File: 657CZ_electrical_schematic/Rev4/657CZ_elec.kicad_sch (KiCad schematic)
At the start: 44 parts, among them M2 Starter, SW1 E-Bus Alt Feed, SW13 E IGN, SW14 M IGN, SW2 Aux Alt Off/On, SW5 BATT/ALT DC POWER

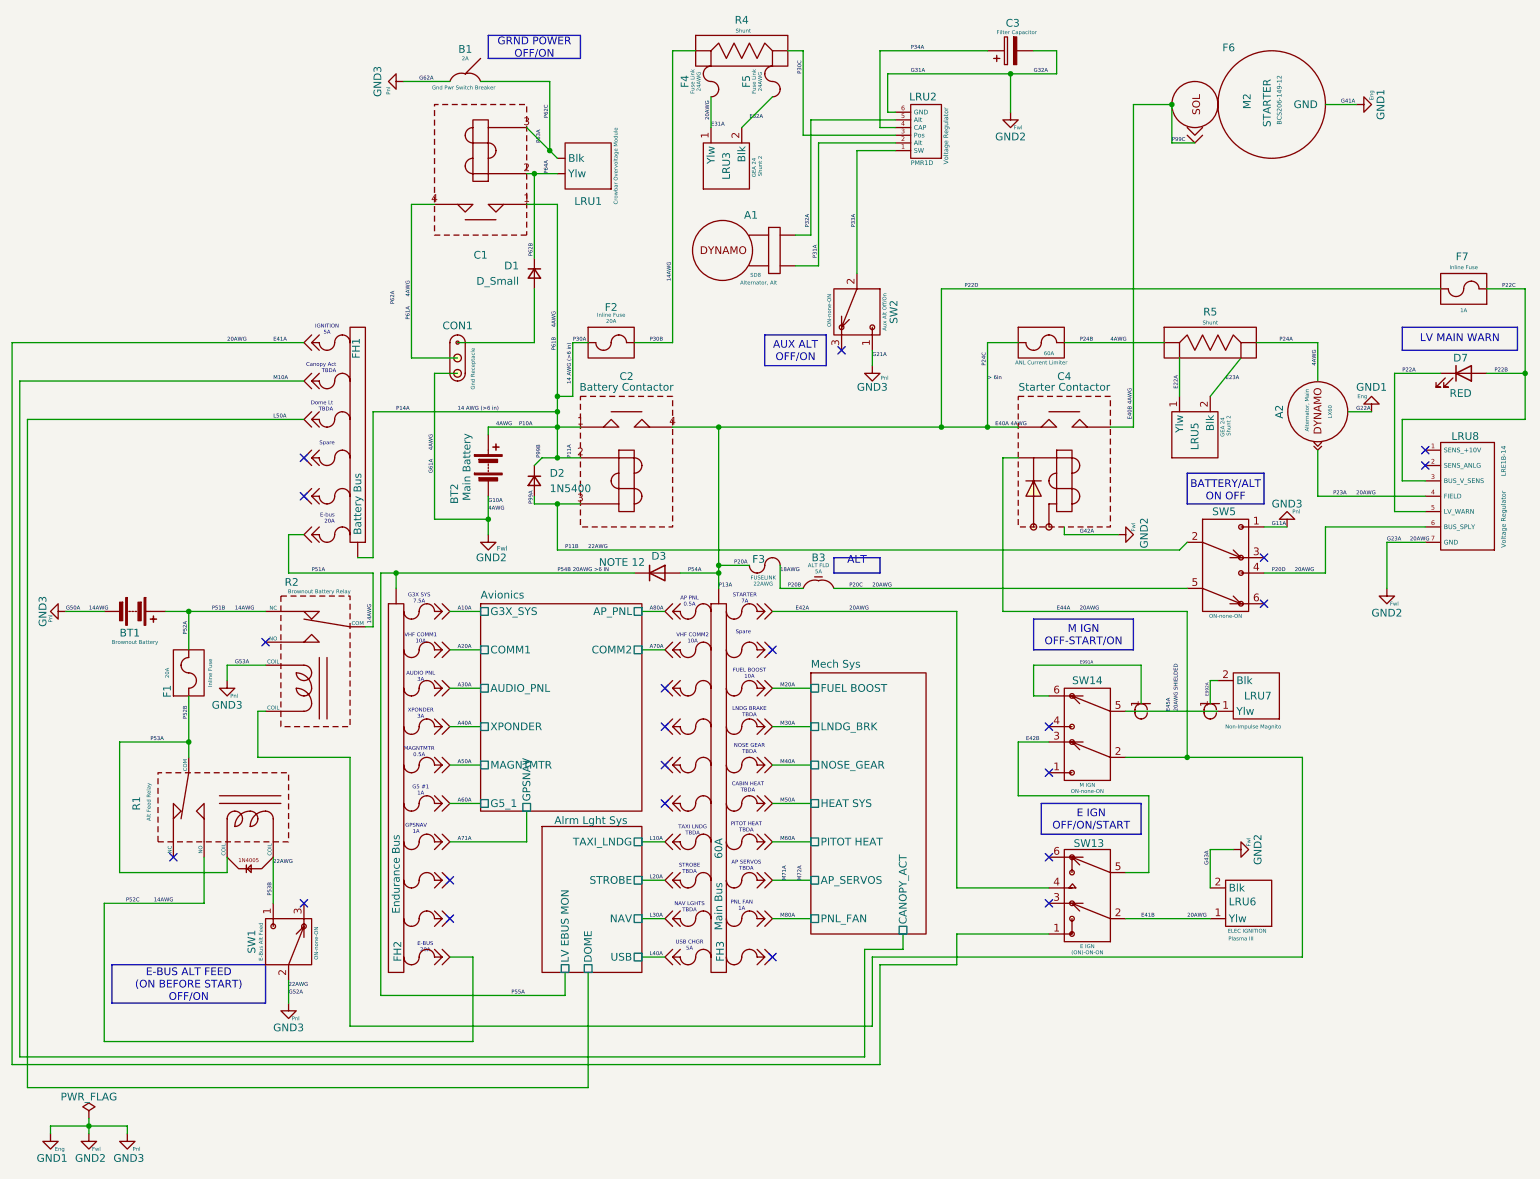
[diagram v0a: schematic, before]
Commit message: corrected comm1,2 to main/ebus, connected lightspeed to ebus
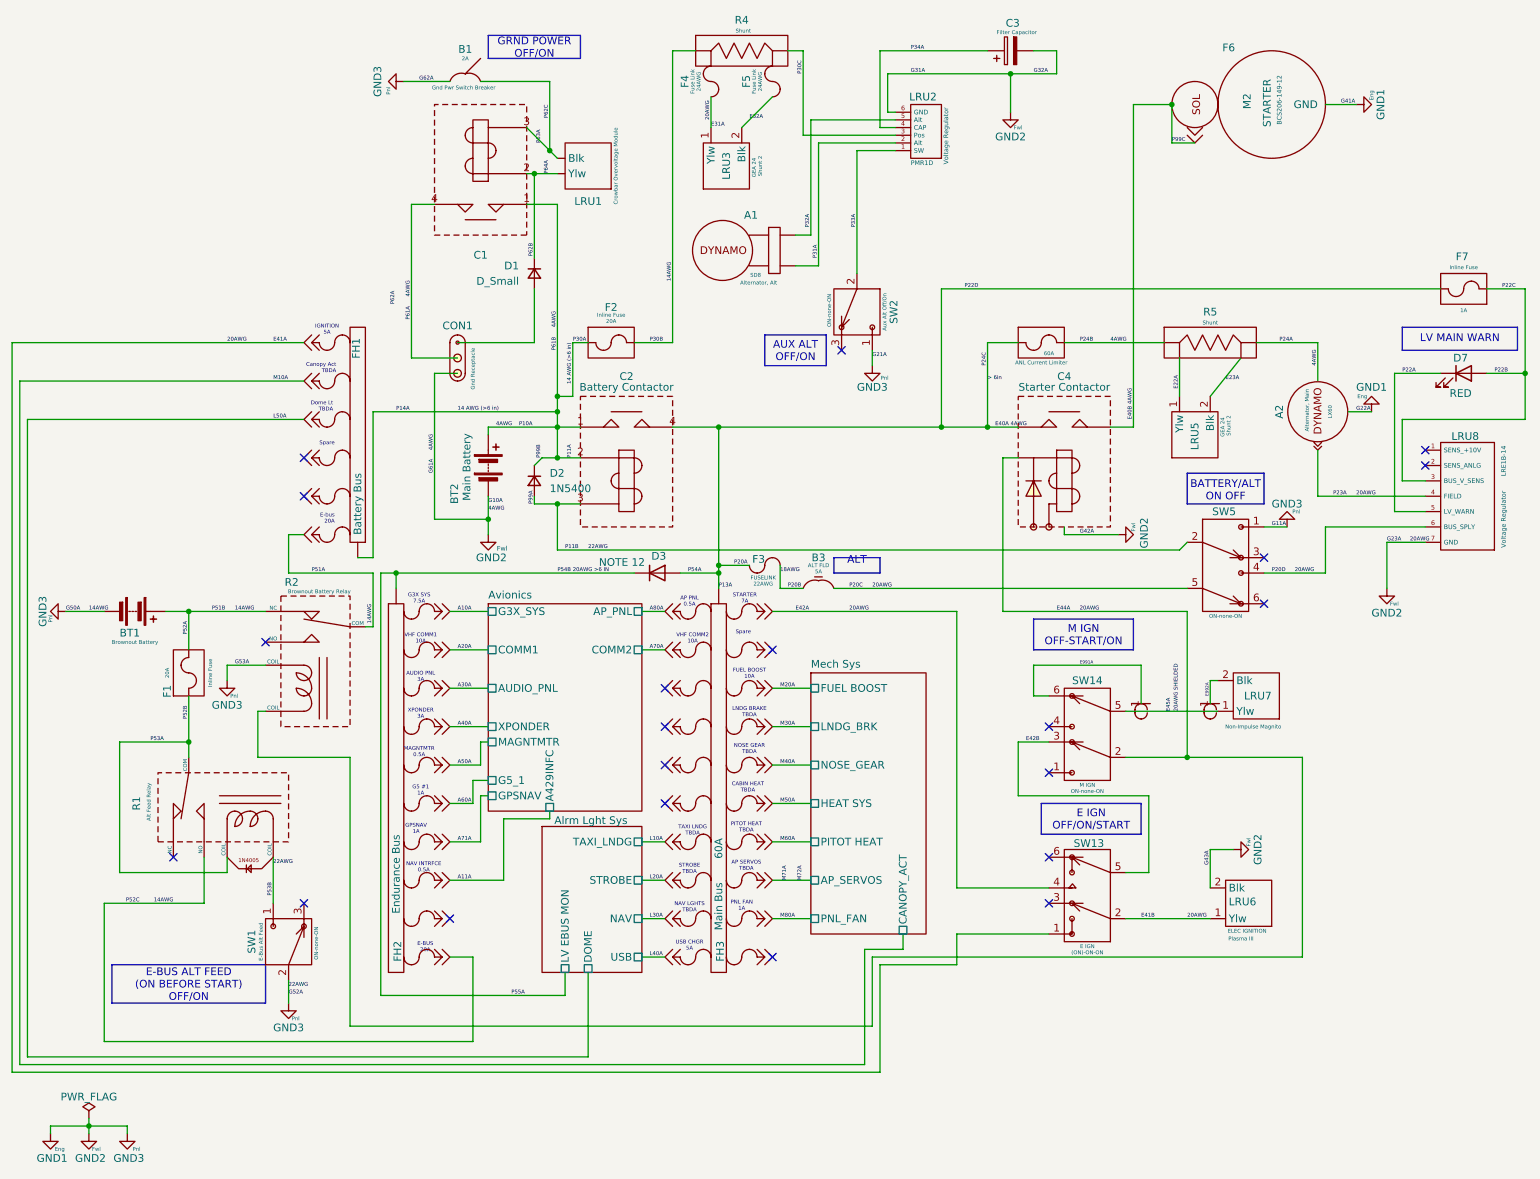
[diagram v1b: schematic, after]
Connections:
- net A11A: now reaches FH2.9 (Desc)
- no-connect marks 22 -> 21
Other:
- sheet Avionics ports: added A429INFC; removed none
- note added: "NAV INTRFCE 0.5A"
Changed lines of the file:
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@@
 		)
 	)
+	(text "NAV INTRFCE\n0.5A"
+		(exclude_from_sim no)
+		(at 82.042 154.178 0)
+		(effects
+			(font
+				(size 0.635 0.635)
+			)
+		)
+	)
 	(text "AP PNL\n0.5A"
 		(exclude_from_sim no)
@@
 	)
 	(no_connect
-		(at 86.36 156.21)
-	)
-	(no_connect
 		(at 62.23 92.71)
 	)
@@
 	(wire
 		(pts
-			(xy 13.97 186.69) (xy 157.48 186.69)
+			(xy 13.97 187.96) (xy 157.48 187.96)
 		)
 		(stroke
@@
 	(wire
 		(pts
-			(xy 86.36 143.51) (xy 91.44 143.51)
+			(xy 86.36 156.21) (xy 95.25 156.21)
+		)
+		(stroke
+			(width 0)
+			(type default)
+		)
+	)
+	(wire
+		(pts
+			(xy 90.17 139.7) (xy 92.71 139.7)
 		)
 		(stroke
@@
 	(wire
 		(pts
-			(xy 86.36 149.86) (xy 99.06 149.86)
+			(xy 86.36 149.86) (xy 91.44 149.86)
 		)
 		(stroke
@@
 	(wire
 		(pts
+			(xy 91.44 133.35) (xy 91.44 137.16)
+		)
+		(stroke
+			(width 0)
+			(type default)
+		)
+	)
+	(wire
+		(pts
 			(xy 100.33 39.37) (xy 104.14 39.37)
 		)
@@
 	(wire
 		(pts
-			(xy 86.36 118.11) (xy 91.44 118.11)
+			(xy 86.36 118.11) (xy 92.71 118.11)
 		)
 		(stroke
@@
 	(wire
 		(pts
-			(xy 154.94 167.64) (xy 154.94 185.42)
+			(xy 154.94 167.64) (xy 154.94 186.69)
 		)
 		(stroke
@@
 	(wire
 		(pts
-			(xy 16.51 190.5) (xy 109.22 190.5)
+			(xy 16.51 185.42) (xy 109.22 185.42)
+		)
+		(stroke
+			(width 0)
+			(type default)
+		)
+	)
+	(wire
+		(pts
+			(xy 95.25 146.05) (xy 102.87 146.05)
 		)
 		(stroke
@@
 	(wire
 		(pts
-			(xy 86.36 111.76) (xy 91.44 111.76)
+			(xy 86.36 111.76) (xy 92.71 111.76)
 		)
 		(stroke
@@
 	(wire
 		(pts
-			(xy 86.36 137.16) (xy 91.44 137.16)
+			(xy 91.44 133.35) (xy 92.71 133.35)
 		)
 		(stroke
@@
 	(wire
 		(pts
-			(xy 15.24 73.66) (xy 15.24 185.42)
+			(xy 15.24 73.66) (xy 15.24 186.69)
 		)
 		(stroke
@@
 	(wire
 		(pts
-			(xy 154.94 185.42) (xy 15.24 185.42)
+			(xy 154.94 186.69) (xy 15.24 186.69)
 		)
 		(stroke
@@
 	(wire
 		(pts
-			(xy 16.51 80.01) (xy 16.51 190.5)
+			(xy 16.51 80.01) (xy 16.51 185.42)
 		)
 		(stroke
@@
 	(wire
 		(pts
+			(xy 91.44 137.16) (xy 86.36 137.16)
+		)
+		(stroke
+			(width 0)
+			(type default)
+		)
+	)
+	(wire
+		(pts
 			(xy 54.61 128.27) (xy 54.61 135.89)
 		)
@@
 	(wire
 		(pts
+			(xy 90.17 139.7) (xy 90.17 143.51)
+		)
+		(stroke
+			(width 0)
+			(type default)
+		)
+	)
+	(wire
+		(pts
 			(xy 227.33 168.91) (xy 156.21 168.91)
 		)
@@
 	(wire
 		(pts
-			(xy 86.36 124.46) (xy 91.44 124.46)
+			(xy 86.36 124.46) (xy 92.71 124.46)
 		)
 		(stroke
@@
 	(wire
 		(pts
+			(xy 91.44 142.24) (xy 92.71 142.24)
+		)
+		(stroke
+			(width 0)
+			(type default)
+		)
+	)
+	(wire
+		(pts
+			(xy 102.87 146.05) (xy 102.87 144.78)
+		)
+		(stroke
+			(width 0)
+			(type default)
+		)
+	)
+	(wire
+		(pts
 			(xy 13.97 67.31) (xy 62.23 67.31)
 		)
@@
 	(wire
 		(pts
-			(xy 13.97 186.69) (xy 13.97 67.31)
+			(xy 13.97 187.96) (xy 13.97 67.31)
 		)
 		(stroke
@@
 	(wire
 		(pts
-			(xy 99.06 149.86) (xy 99.06 144.78)
+			(xy 91.44 149.86) (xy 91.44 142.24)
 		)
 		(stroke
@@
 	(wire
 		(pts
+			(xy 90.17 143.51) (xy 86.36 143.51)
+		)
+		(stroke
+			(width 0)
+			(type default)
+		)
+	)
+	(wire
+		(pts
 			(xy 247.65 95.25) (xy 242.57 95.25)
 		)
@@
 	(wire
 		(pts
-			(xy 86.36 130.81) (xy 91.44 130.81)
+			(xy 86.36 130.81) (xy 92.71 130.81)
 		)
 		(stroke
@@
 	(wire
 		(pts
-			(xy 109.22 190.5) (xy 109.22 171.45)
+			(xy 109.22 185.42) (xy 109.22 171.45)
 		)
 		(stroke
@@
 	(wire
 		(pts
+			(xy 95.25 156.21) (xy 95.25 146.05)
+		)
+		(stroke
+			(width 0)
+			(type default)
+		)
+	)
+	(wire
+		(pts
 			(xy 187.96 67.31) (xy 204.47 67.31)
 		)
@@
 	(wire
 		(pts
-			(xy 157.48 170.18) (xy 157.48 186.69)
+			(xy 157.48 170.18) (xy 157.48 187.96)
 		)
 		(stroke
@@
 		)
 	)
+	(label "A11A"
+		(at 87.63 156.21 0)
+		(effects
+			(font
+				(size 0.635 0.635)
+			)
+			(justify left bottom)
+		)
+	)
 	(label "E42A"
 		(at 143.51 111.76 0)
@@
 	)
 	(sheet
-		(at 91.44 110.49)
-		(size 26.67 34.29)
+		(at 92.71 110.49)
+		(size 25.4 34.29)
 		(exclude_from_sim no)
 		(in_bom yes)
@@
 		)
 		(property "Sheetname" "Avionics"
-			(at 91.44 109.7784 0)
+			(at 92.71 109.7784 0)
 			(effects
 				(font
@@
 		)
 		(property "Sheetfile" "avionics.kicad_sch"
-			(at 91.44 145.3646 0)
+			(at 92.71 145.3646 0)
 			(effects
 				(font
@@
 		)
 		(pin "AUDIO_PNL" passive
-			(at 91.44 124.46 180)
+			(at 92.71 124.46 180)
 			(effects
 				(font
@@
 		)
 		(pin "XPONDER" passive
-			(at 91.44 130.81 180)
+			(at 92.71 130.81 180)
 			(effects
 				(font
@@
 		)
 		(pin "MAGNTMTR" passive
-			(at 91.44 137.16 180)
+			(at 92.71 133.35 180)
 			(effects
 				(font
@@
 		)
 		(pin "G3X_SYS" passive
-			(at 91.44 111.76 180)
+			(at 92.71 111.76 180)
 			(effects
 				(font
@@
 		)
 		(pin "G5_1" passive
-			(at 91.44 143.51 180)
+			(at 92.71 139.7 180)
 			(effects
 				(font
@@
 		)
 		(pin "COMM1" passive
-			(at 91.44 118.11 180)
+			(at 92.71 118.11 180)
 			(effects
 				(font
@@
 		)
 		(pin "GPSNAV" passive
-			(at 99.06 144.78 270)
+			(at 92.71 142.24 180)
+			(effects
+				(font
+					(size 1.27 1.27)
+				)
+				(justify left)
+			)
+		)
+		(pin "A429INFC" passive
+			(at 102.87 144.78 270)
 			(effects
 				(font
